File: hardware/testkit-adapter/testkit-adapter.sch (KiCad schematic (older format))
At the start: 27 parts, among them J1 LEFT, J2 RIGHT, J3 SWD, J4 Left, J5 Bottom, J6 Right

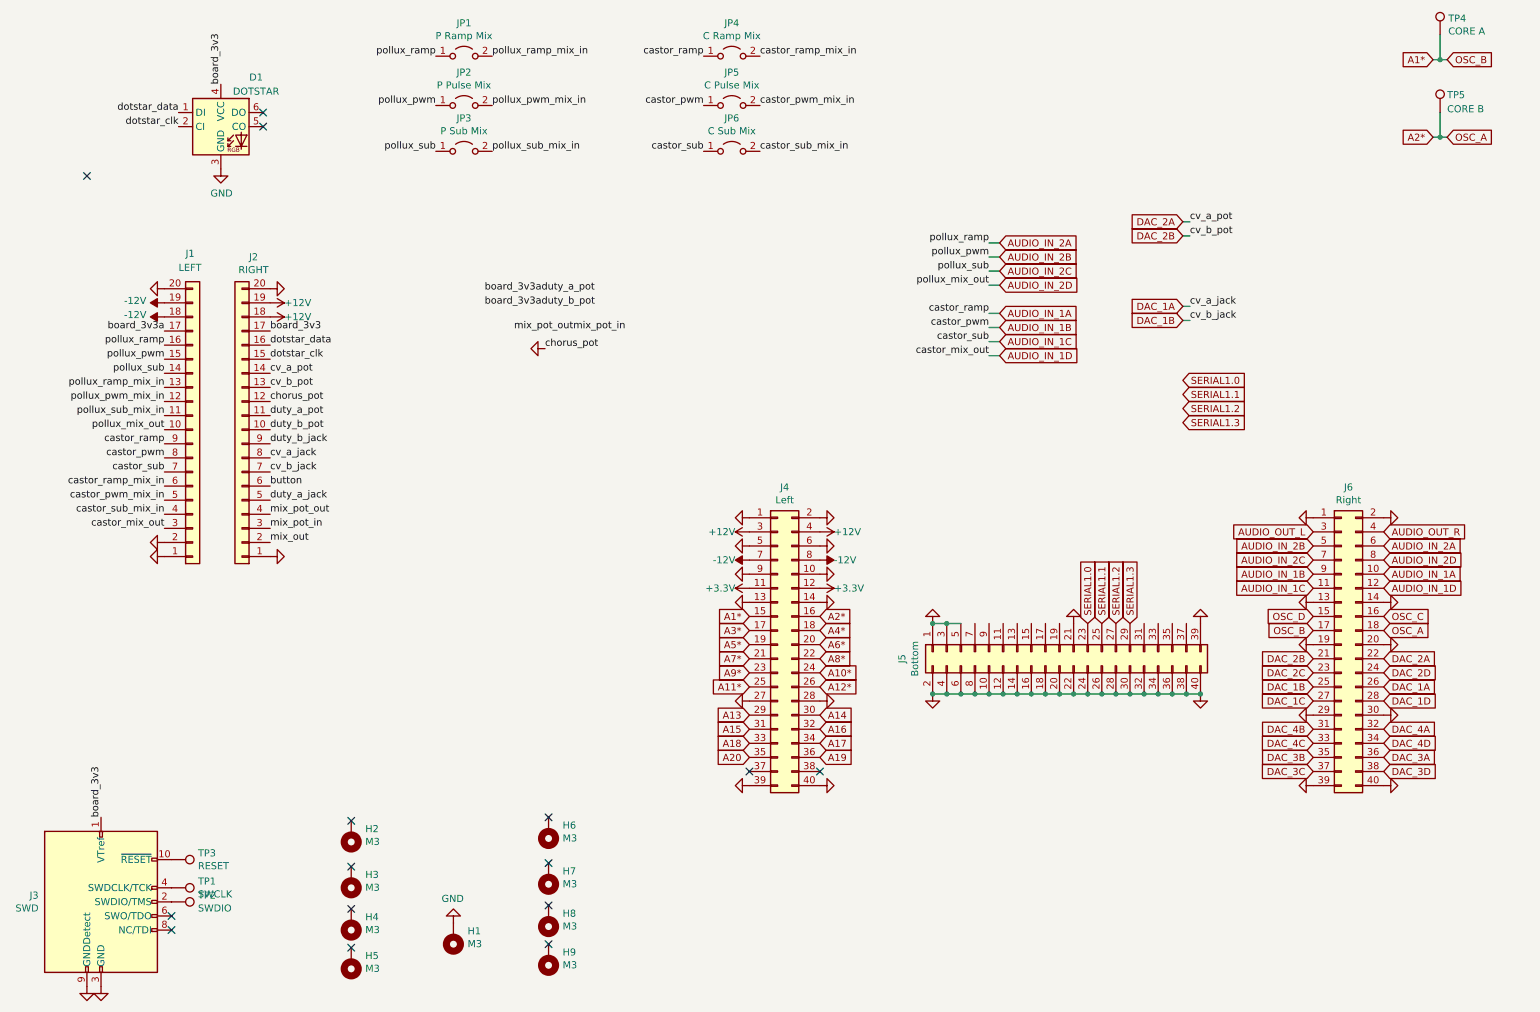
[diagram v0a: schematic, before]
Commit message: hardware/testkit-adapter: Add laser designs for pin holder, board guide, and pressure plate
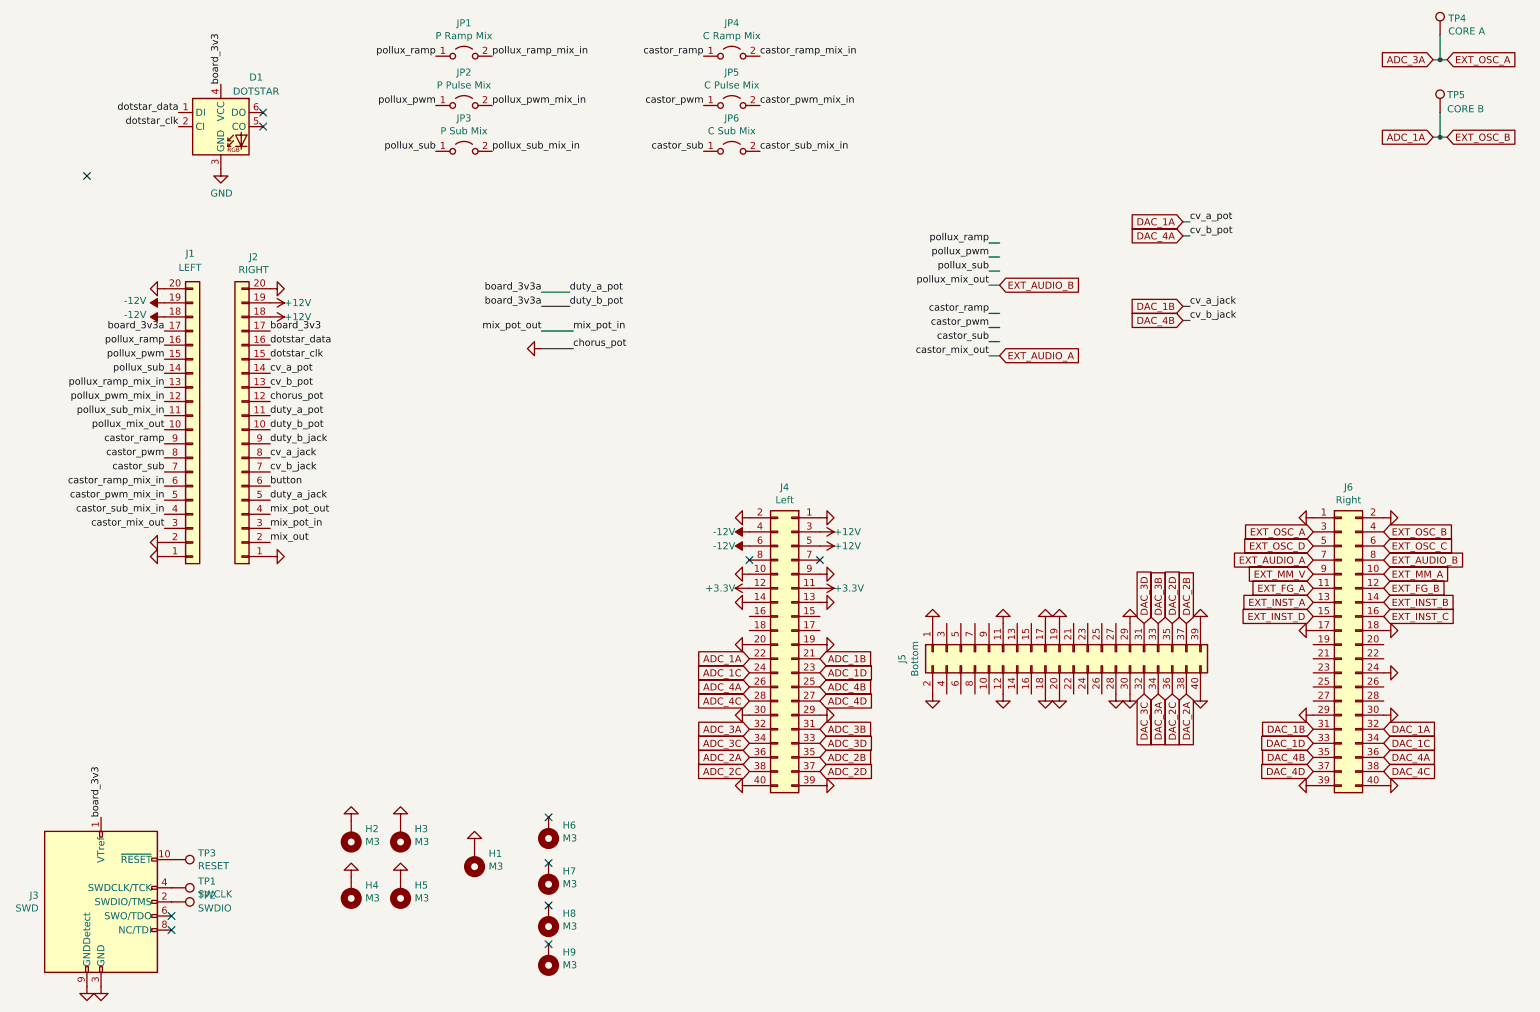
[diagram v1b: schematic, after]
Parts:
- H2, H3, H4, H5: footprint MountingHole:MountingHole_3.2mm_M3 -> MountingHole:MountingHole_3.2mm_M3_Pad_Via
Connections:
- net labels added: ADC_1A, ADC_1B, ADC_1C, ADC_1D, ADC_2A, ADC_2B, ADC_2C, ADC_2D, ADC_3A, ADC_3B, ADC_3C, ADC_3D, ADC_4A, ADC_4B, ADC_4C, ADC_4D, EXT_AUDIO_A, EXT_AUDIO_B, EXT_FG_A, EXT_FG_B, EXT_INST_A, EXT_INST_B, EXT_INST_C, EXT_INST_D, EXT_MM_A, EXT_MM_V, EXT_OSC_A, EXT_OSC_B, EXT_OSC_C, EXT_OSC_D
- net labels removed: A1*, A10*, A11*, A12*, A13, A14, A15, A16, A17, A18, A19, A2*, A20, A3*, A4*, A5*, A6*, A7*, A8*, A9*, AUDIO_IN_1A, AUDIO_IN_1B, AUDIO_IN_1C, AUDIO_IN_1D, AUDIO_IN_2A, AUDIO_IN_2B, AUDIO_IN_2C, AUDIO_IN_2D, AUDIO_OUT_L, AUDIO_OUT_R, OSC_A, OSC_B, OSC_C, OSC_D, SERIAL1.0, SERIAL1.1, SERIAL1.2, SERIAL1.3
- wire segments 39 -> 22
- no-connect marks 15 -> 11
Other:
- moved on the sheet: H1, H3, H4, H5
